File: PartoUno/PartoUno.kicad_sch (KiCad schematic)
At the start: 71 parts, among them J10 RED5, J11 GRE3, J12 GRE2, J13 RED4, J14 GNC_BOND, J15 GNC_BOND, J16 GNC_BOND, J17 GNC_BOND, J18 GNC_BOND, J19 GNC_BOND, J2 WHI3, J20 GNC_BOND, J21 GNC_BOND, J22 GNC_BOND, J23 GNC_BOND, J24 GNC_BOND, J25 GNC_BOND, J26 GNC_BOND, J27 GNC_BOND, J28 GNC_BOND, J29 GNC_BOND, J3 YEL5, J30 GNC_BOND, J31 GNC_BOND, J32 GNC_BOND, J33 GNC_BOND, J34 GNC_BOND, J35 GNC_BOND, J4 BLU1, J5 BLU2, J6 YEL4, J7 WHI4, J8 YEL3, J9 GRE1, U1 ATtiny45V-10S, U2 74HC595, U3 74HC595, U4 74HC595

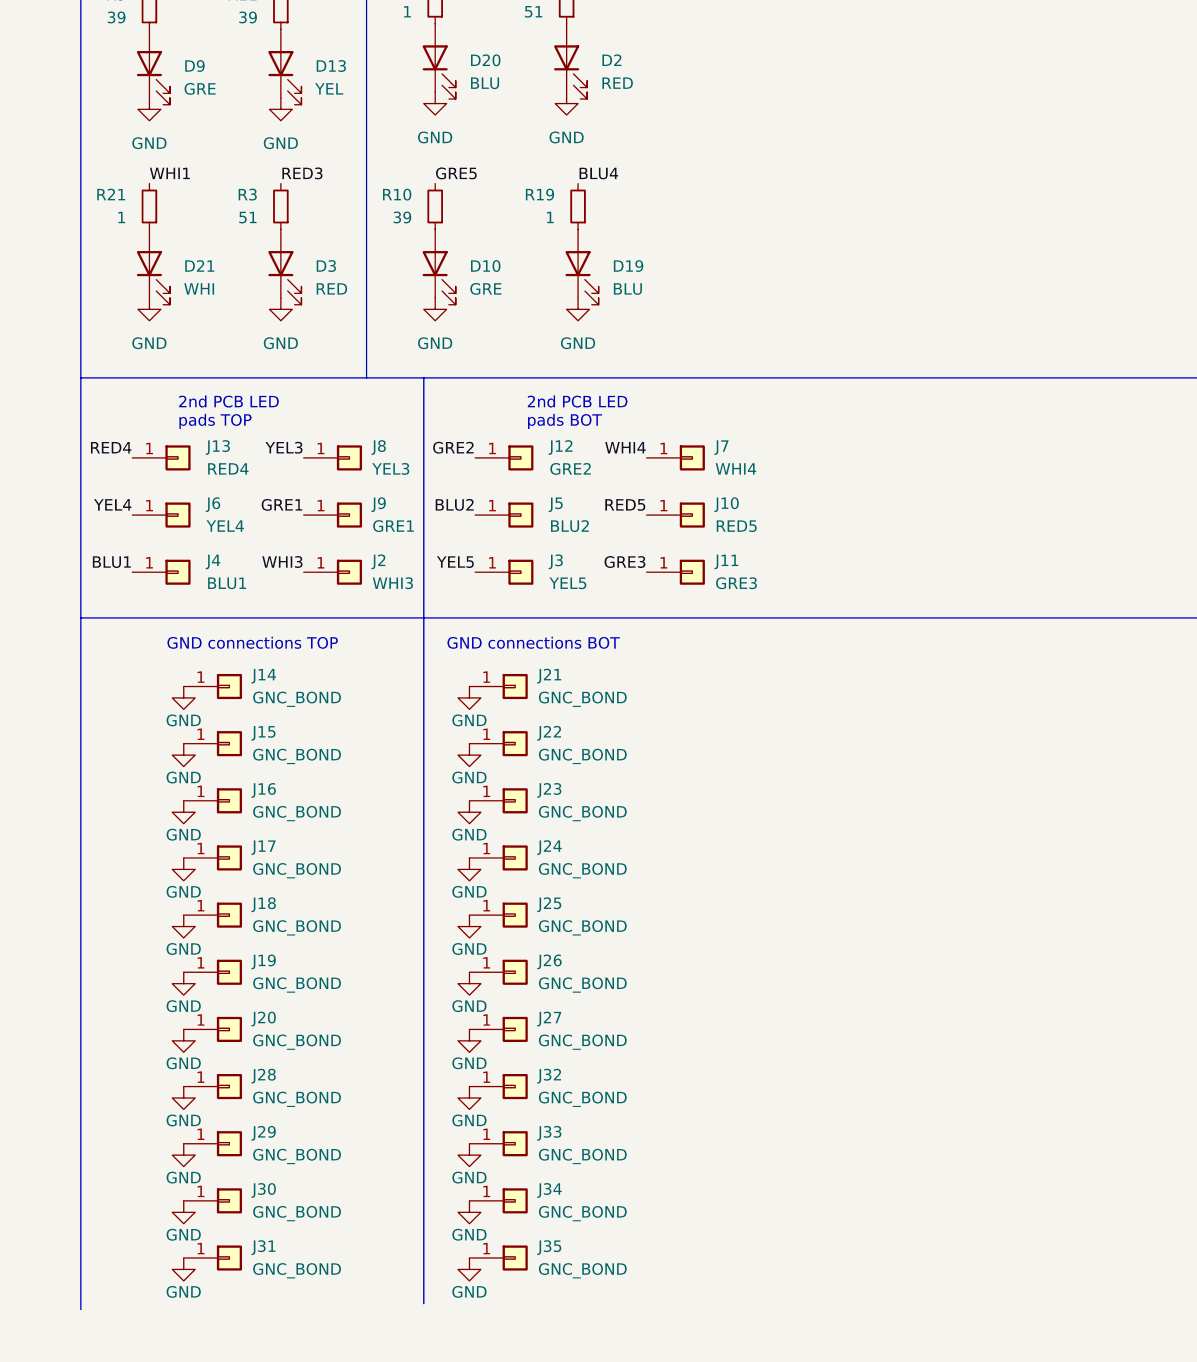
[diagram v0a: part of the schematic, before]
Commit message: Fixed code
Had an issue in shiftOutData where I defined the wrong data type (16 bit instead of 32 bit) so it cut all data short
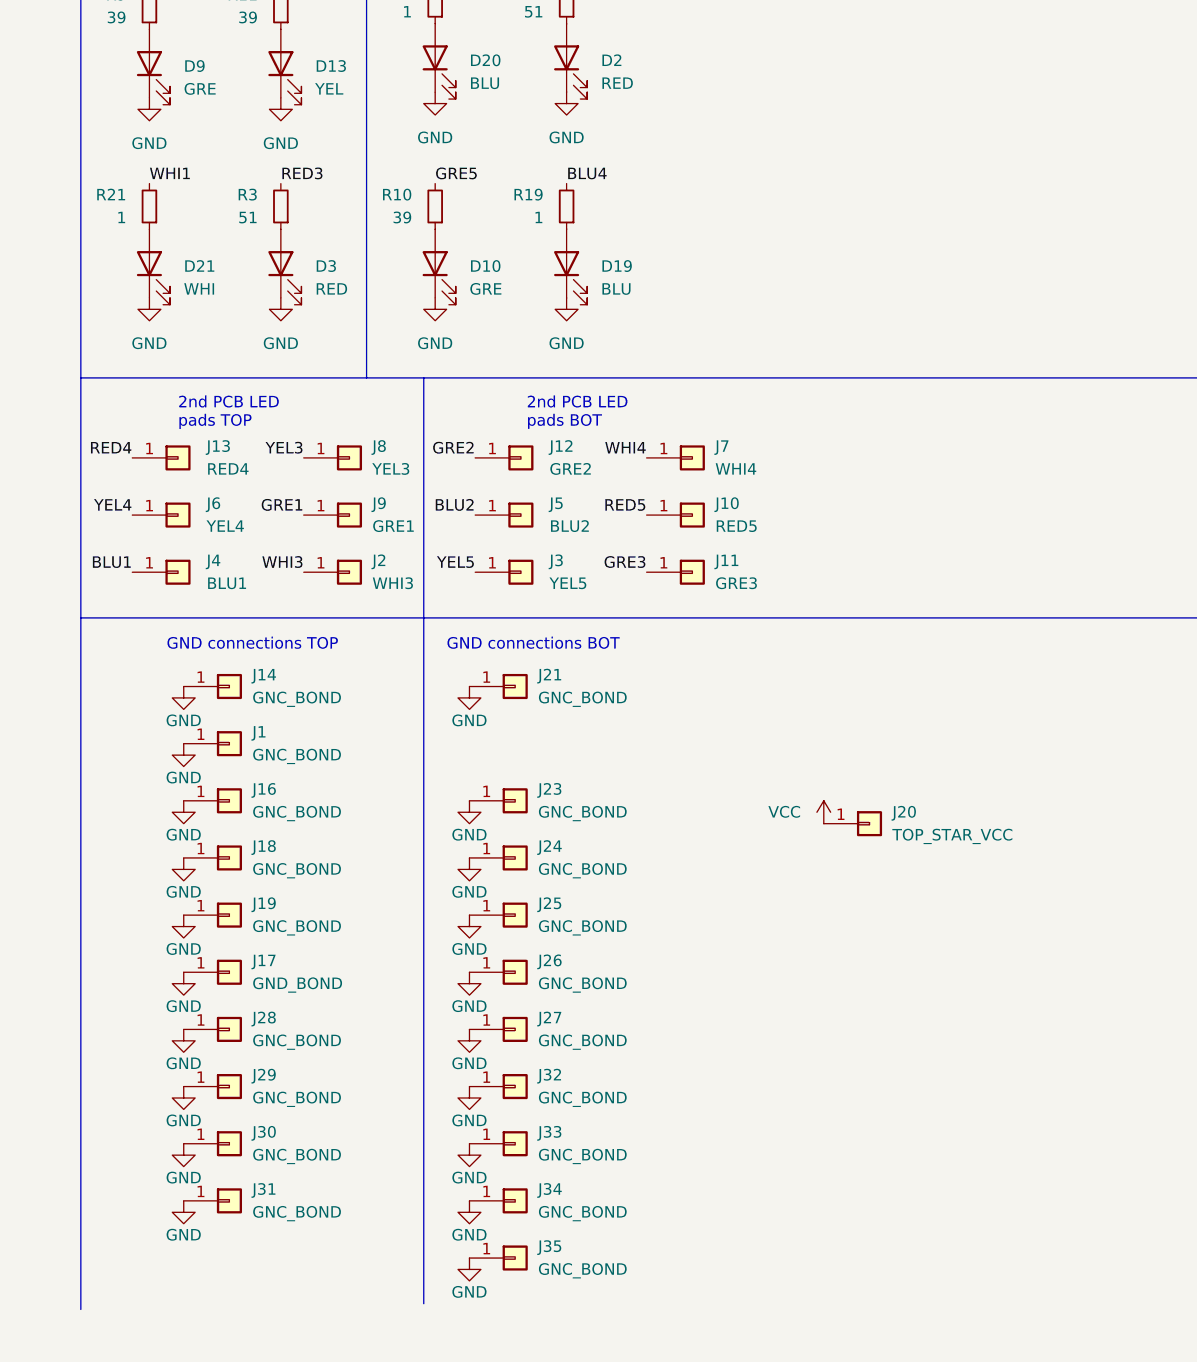
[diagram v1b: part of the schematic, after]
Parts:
- removed J15, J22: GNC_BOND, Connector_Wire:SolderWirePad_1x01_SMD_1x2mm, symbol Connector_Generic:Conn_01x01
- added J1: GNC_BOND, Connector_Wire:SolderWirePad_1x01_SMD_1x2mm, symbol Connector_Generic:Conn_01x01
- J17: value GNC_BOND -> GND_BOND
- J20: value GNC_BOND -> TOP_STAR_VCC
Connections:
- net GND: now also J1.1 (Pin_1); no longer J20.1 (Pin_1)
- net VCC: now also J20.1 (Pin_1)
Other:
- moved on the sheet: D19, J17, J18, J19, J20, J28, J29, J30, J31, R19

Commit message: Updated design
+ top LED
+ power switch
~ routing
~ via stitching more aligned
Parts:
- removed J14, J25, J30, J31: GNC_BOND, Connector_Wire:SolderWirePad_1x01_SMD_1x2mm, symbol Connector_Generic:Conn_01x01
- removed J17: GND_BOND, Connector_Wire:SolderWirePad_1x01_SMD_1x2mm, symbol Connector_Generic:Conn_01x01
- added SW1: ON/OFF, Button_Switch_SMD:SW_DIP_SPSTx01_Slide_6.7x4.1mm_W6.73mm_P2.54mm_LowProfile_JPin, symbol Switch:SW_SPST
- BT1: footprint custom:2032 battery narrow -> custom:2032 battery clip
- renumbered C3 to C2, C2 to C3, D9 to D1, D22 to D10, D2 to D11, D19 to D12, D21 to D2, D1 to D3, D18 to D4, D13 to D5, D3 to D6, D14 to D7, D20 to D8, D10 to D9, J13 to J1, J8 to J10, J9 to J11, J2 to J12, J21 to J13, J23 to J14, J24 to J15, J26 to J16, J27 to J17, J32 to J18, J33 to J19, J6 to J2, J34 to J20, J35 to J21, J12 to J22, J5 to J23, J3 to J24, J7 to J25, J10 to J26, J11 to J27, J20 to J28, J4 to J3, J1 to J4, J16 to J5, J18 to J6, J19 to J7, J28 to J8, J29 to J9, R25 to R1, R22 to R11, R2 to R12, R19 to R13, R9 to R2, R21 to R3, R1 to R4, R18 to R5, R11 to R6, R3 to R7, R12 to R8, R20 to R9
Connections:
- net VCC: now also SW1.2 (B); no longer BT1.1 (+)
- new net: BT1.1 (+), SW1.1 (A)
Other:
- moved on the sheet: BT1, J14, J15, J16, J17, J18, J19, J20, J21, J4, J5, J6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
